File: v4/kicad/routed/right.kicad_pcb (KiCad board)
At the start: 2 copper layers, 160 x 118.6 mm, 72 parts

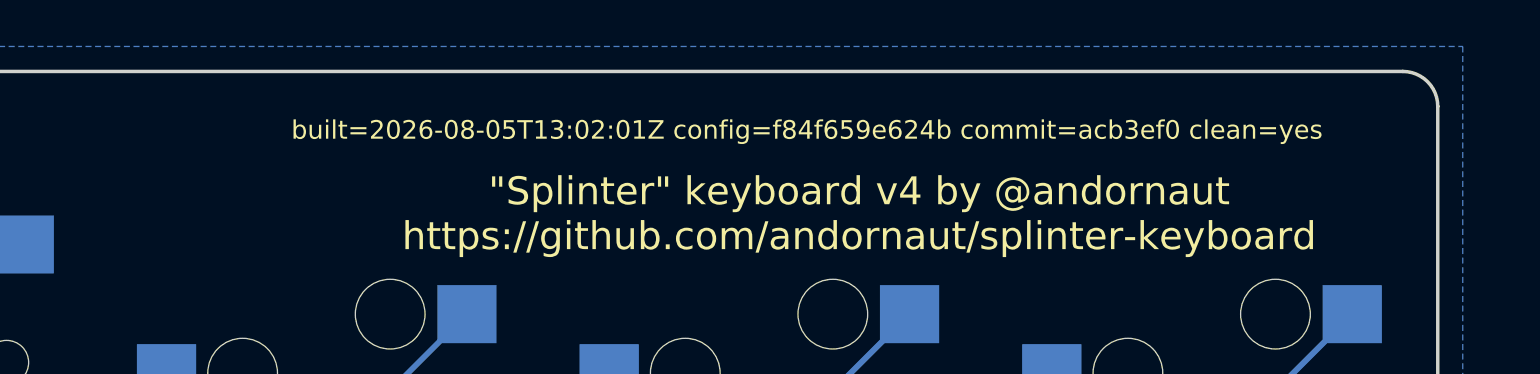
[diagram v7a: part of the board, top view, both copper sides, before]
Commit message: Restamp the boards against the reworked config comment
The stamp keys on the config hash alone, so correcting the comment above
_wallsleft_unfilleted moved every board to stale. Nothing about the design
changed: teardrops hold at 288 left and 303 right, segments at 318 and 334, and
the diff is the stamp plus regenerated UUIDs.

Built from a clean tree so commit= names the source these boards came from.
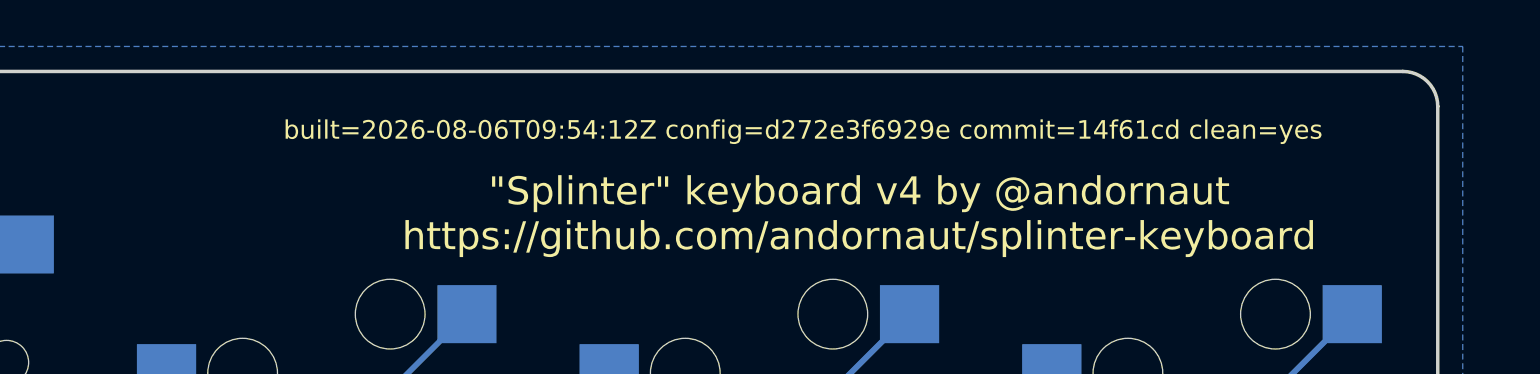
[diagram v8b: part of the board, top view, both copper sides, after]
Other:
- board text added: "built=2026-08-06T09:54:12Z config=d272e3f6929e commit=14f61cd clean=yes"
- board text removed: "built=2026-08-05T13:02:01Z config=f84f659e624b commit=acb3ef0 clean=yes"
